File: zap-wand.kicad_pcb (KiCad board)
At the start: 2 copper layers, 12 x 25 mm, 14 parts, among them IC1 NC7WZ02, Q1 Q_PMOS_GDS, SW1 SW_PUSH_SMALL, U1 NCP103

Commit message: Various tweaks and fixes
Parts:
- removed RV1: 100k, parts:PVZ2A
- added R4: 10k, agg:0603, F.Cu at (69.9, 40.0)
- added R5: 18k, agg:0603, F.Cu at (62.5, 38.4)
- BATT1: footprint agg:SM02B-PASS -> agg:SIL-254P-02
- C1, C3, C4, R1, R3: footprint agg:0805 -> agg:0603
- C2: value 47u -> 10n
- D1: footprint LEDs:LED-5MM -> agg:SIL-254P-02
- R2: value 100k -> 820k; footprint agg:0805 -> agg:0603
- moved C3 5.43 mm to (67.4, 40.1), turned to 90 degrees
- moved R1 4.03 mm to (69.2, 37.6), turned to 90 degrees
- moved U1 3.87 mm to (65.6, 39.7), turned to 0 degrees
- moved IC1 3.25 mm to (66.5, 36.1)
- moved C2 3.02 mm to (63.5, 35.9)
- moved C4 2.98 mm to (64.6, 40.1), turned to 270 degrees
- moved C1 2.91 mm to (70.7, 37.6), turned to 270 degrees
- moved R2 2.09 mm to (61.8, 36.1), turned to 90 degrees
- moved Q1 1.99 mm to (69.9, 33.6)
- moved D1 1.24 mm to (66.2, 31.5)
- moved R3 0.90 mm to (70.1, 31.5), turned to 0 degrees
- moved SW1 0.50 mm to (62.8, 42.0)
- moved BATT1 0.25 mm to (66.0, 49.5), turned to 0 degrees
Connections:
- R2 pad 1: +3V3 -> Net-(R2-Pad1)
- R2 pad 2: Net-(R2-Pad2) -> Net-(C2-Pad1)
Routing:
- net +3V3: track 26.3 -> 19.8 mm
- net Net-(BATT1-Pad1): track 3.87 -> 9.35 mm
- net Net-(C2-Pad1): track 8.49 -> 4.14 mm
- net GND: track 7.90 -> 5.89 mm
- net Net-(C1-Pad1): track 4.59 -> 2.87 mm
- net Net-(R2-Pad2): track 1.68 -> 0.00 mm
- net Net-(C1-Pad2): track 7.14 -> 8.67 mm
- net Net-(R2-Pad1): track 0.00 -> 1.50 mm
- net Net-(D1-Pad2): track 2.60 -> 1.80 mm
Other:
- board size 12 x 25 mm -> 12 x 21 mm
- board text added: "+"
- board text added: "-"
- board text added: "Zap Wand V1 pcb@harkonen.net 19/07/16 git.io/vKoew"
- board text removed: "Fast"
- board text removed: "Slow"

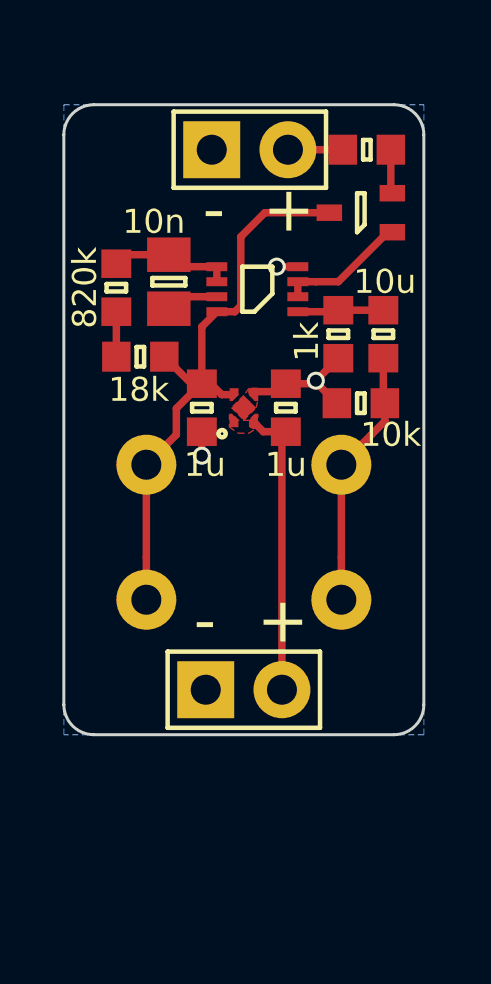
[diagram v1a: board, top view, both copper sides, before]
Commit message: Beefier regulator, pcb shuffle
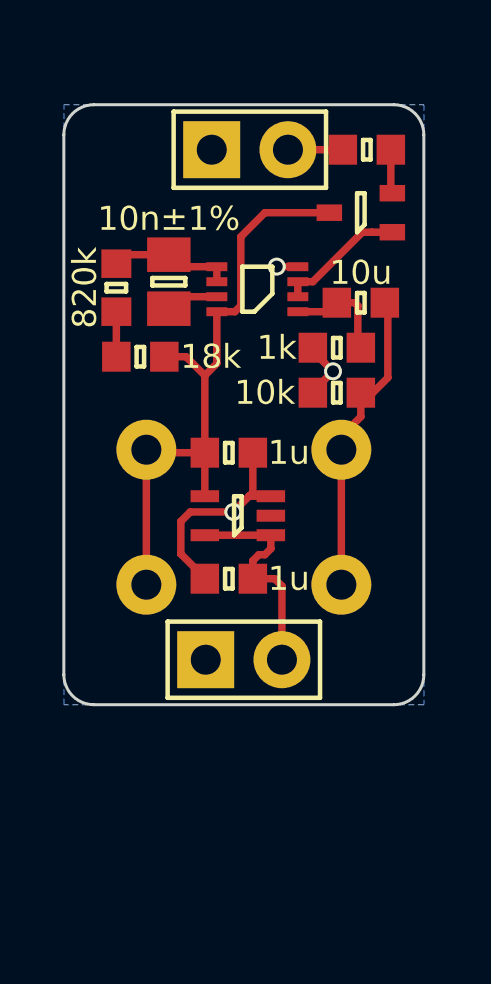
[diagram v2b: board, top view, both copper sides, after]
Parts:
- C2: value 10n -> 10n±1%
- U1: value NCP103 -> NCP4683DSQ33T1G; footprint parts:UDFN4 -> agg:SC-70-5
- moved C3 6.01 mm to (65.5, 45.8), turned to 180 degrees
- moved U1 4.04 mm to (65.8, 43.7), turned to 180 degrees
- moved C4 1.75 mm to (65.5, 41.6), turned to 0 degrees
- moved C1 1.29 mm to (69.9, 36.6), turned to 0 degrees
- moved BATT1 1.00 mm to (66.0, 48.5)
- moved R4 0.87 mm to (69.1, 39.6)
- moved SW1 0.50 mm to (62.8, 41.5)
- moved R1 0.45 mm to (69.1, 38.1), turned to 0 degrees
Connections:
- U1 pad 2: Net-(BATT1-Pad1) -> Net-(U1-Pad2)
- U1 pad 5: GND -> Net-(BATT1-Pad1)
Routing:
- net GND: track 5.89 -> 9.85 mm
- net Net-(C1-Pad2): track 8.67 -> 11.1 mm
- net Net-(BATT1-Pad1): track 9.35 -> 7.54 mm
- net +3V3: track 19.8 -> 20.9 mm
- net Net-(C1-Pad1): track 2.87 -> 3.61 mm
- removed copper zone on F.Cu, net GND
- removed copper zone on F.Cu, net Net-(BATT1-Pad1)
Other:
- board size 12 x 21 mm -> 12 x 20 mm
- board text added: "BATT"
- board text added: "LED"
